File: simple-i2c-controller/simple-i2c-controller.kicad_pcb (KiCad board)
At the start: 2 copper layers, 10 parts, among them P1 CONN_VCC_IN, P2 I2C, P3 CONN_VCC, P4 CONN_5V, U1 ARDUINO_NANO

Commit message: [simple-i2c-controller]
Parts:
- moved P4 0.89 mm to (126.0, 54.6)
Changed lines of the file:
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@@
   )
   (module PINHEAD1-2-UP (layer F.Cu)
-    (at 125.095 54.61 90)
+    (at 125.984 54.61 90)
     (attr virtual)
     (fp_text reference P4 (at -1.905 -3.81 90) (layer F.SilkS)
@@
   (segment (start 131.826 56.896) (end 131.826 51.816) (width 0.508) (layer B.Cu) (net 1))
   (segment (start 133.35 58.42) (end 131.826 56.896) (width 0.508) (layer B.Cu) (net 1))
+  (segment (start 125.73 59.69) (end 125.73 59.436) (width 0.508) (layer B.Cu) (net 2))
+  (segment (start 128.651 56.515) (end 128.651 53.975) (width 0.508) (layer B.Cu) (net 2))
+  (segment (start 125.73 59.436) (end 128.651 56.515) (width 0.508) (layer B.Cu) (net 2))
   (segment (start 125.095 53.34) (end 122.936 53.34) (width 0.508) (layer B.Cu) (net 2))
   (segment (start 130.81 36.83) (end 130.81 33.02) (width 0.508) (layer B.Cu) (net 2))
@@
   (segment (start 122.936 53.34) (end 122.809 53.467) (width 0.508) (layer B.Cu) (net 2))
   (segment (start 125.095 53.34) (end 128.016 53.34) (width 0.508) (layer B.Cu) (net 2))
-  (segment (start 125.73 58.42) (end 125.73 59.69) (width 0.508) (layer B.Cu) (net 2))
-  (segment (start 128.651 55.499) (end 125.73 58.42) (width 0.508) (layer B.Cu) (net 2))
-  (segment (start 128.651 53.975) (end 128.651 55.499) (width 0.508) (layer B.Cu) (net 2))
   (segment (start 128.016 53.34) (end 128.651 53.975) (width 0.508) (layer B.Cu) (net 2))
   (segment (start 130.81 59.69) (end 130.81 57.785) (width 0.508) (layer B.Cu) (net 3))
@@
   (segment (start 123.317 49.53) (end 122.047 50.8) (width 0.508) (layer B.Cu) (net 4))
   (segment (start 126.873 49.53) (end 123.317 49.53) (width 0.508) (layer B.Cu) (net 4))
-  (segment (start 128.27 59.69) (end 128.27 57.785) (width 0.508) (layer B.Cu) (net 4))
+  (segment (start 128.27 59.69) (end 128.27 58.801) (width 0.508) (layer B.Cu) (net 4))
   (segment (start 122.047 50.8) (end 120.65 50.8) (width 0.508) (layer B.Cu) (net 4))
-  (segment (start 129.794 56.261) (end 129.794 52.451) (width 0.508) (layer B.Cu) (net 4))
-  (segment (start 128.27 57.785) (end 129.794 56.261) (width 0.508) (layer B.Cu) (net 4))
+  (segment (start 129.794 57.277) (end 129.794 52.451) (width 0.508) (layer B.Cu) (net 4))
+  (segment (start 128.27 58.801) (end 129.794 57.277) (width 0.508) (layer B.Cu) (net 4))
   (segment (start 134.62 55.88) (end 137.16 55.88) (width 1.27) (layer B.Cu) (net 5))
   (segment (start 132.715 40.005) (end 128.27 40.005) (width 1.27) (layer B.Cu) (net 5))

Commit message: [simple-i2c-controller] Added pull-up resistors to i2c bus.
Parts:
- added R1: 10k, R3-LARGE_PADS, F.Cu at (129.4, 50.4)
- added R2: 10k, R3-LARGE_PADS, F.Cu at (117.5, 44.5)
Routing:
- net +5V: track 43.7 -> 49.5 mm
- net N-0000025: track 19.4 -> 22.3 mm
- net VCC: track 44.1 -> 45.4 mm
- net N-000006: track 18.8 -> 17.6 mm
- net GND: track 72.1 -> 72.9 mm
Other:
- board text added: "SIMPLE I C Controller v1.1"
- board text removed: "SIMPLE I C Controller v1.0"

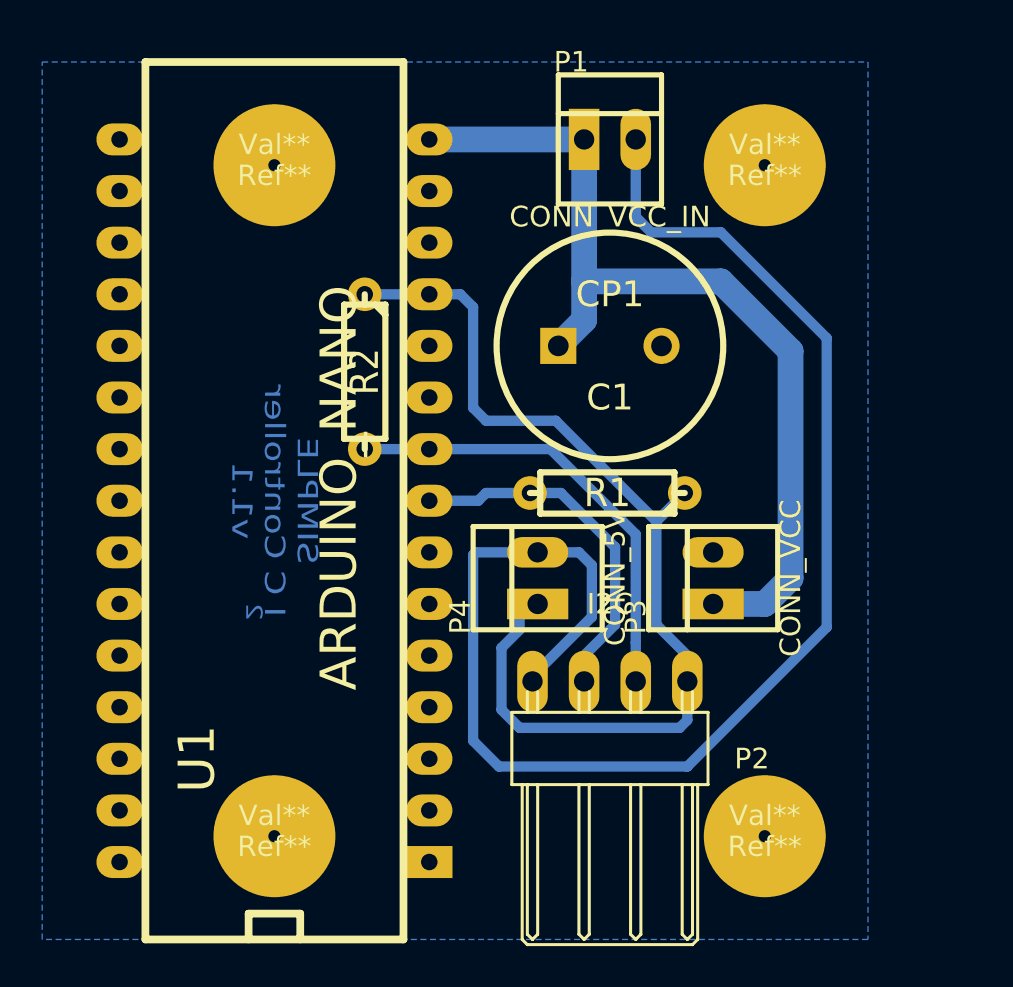
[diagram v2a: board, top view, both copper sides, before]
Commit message: [simple-i2c-controller] Screw holes enlarged and rearranged.
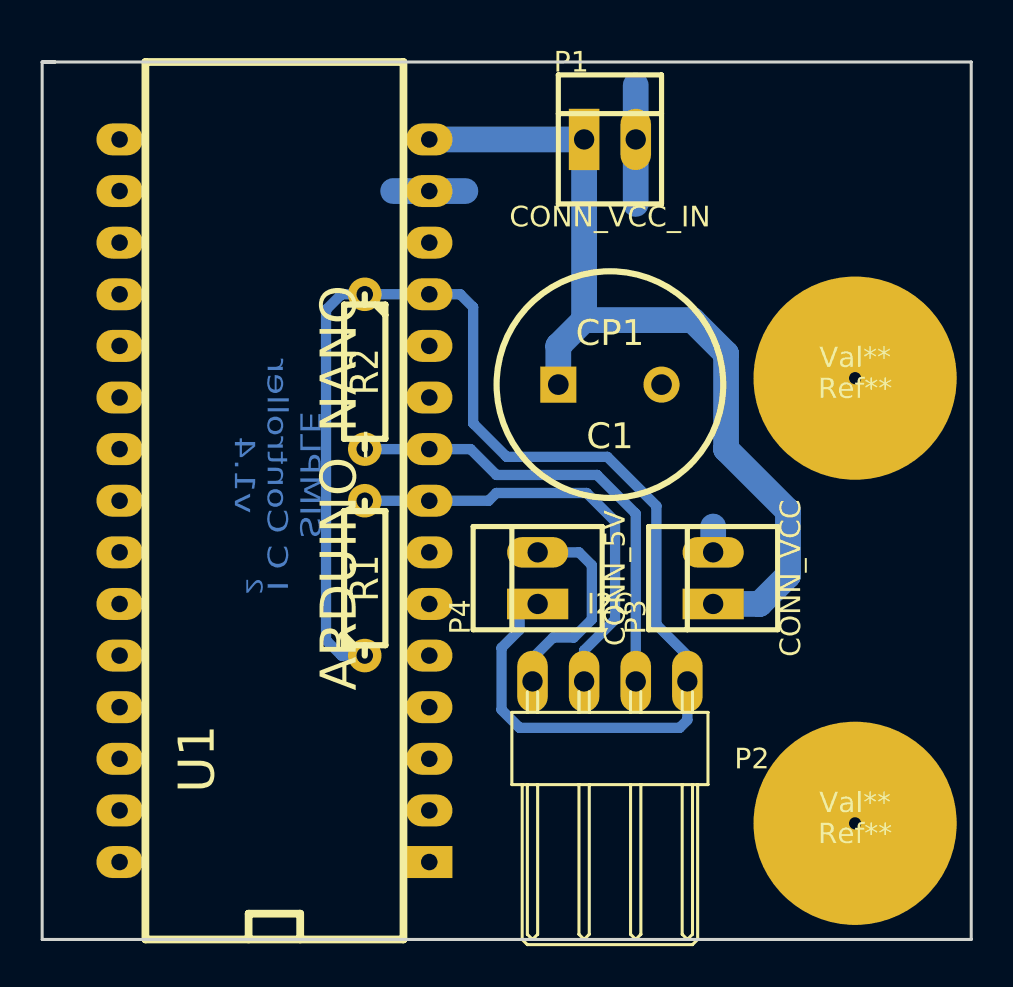
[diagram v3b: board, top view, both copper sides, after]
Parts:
- removed the Ref** at (113.0, 34.3)
- removed the Ref** at (137.2, 67.3)
- removed the Ref** at (113.0, 67.3)
- added Ref**: Val**, pad, F.Cu at (141.6, 66.7)
- moved R1 12.7 mm to (117.5, 54.6), turned to 90 degrees
- moved Ref** 11.4 mm to (141.6, 44.8)
- moved C1 1.91 mm to (129.5, 45.1)
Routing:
- net GND: track 72.9 -> 21.1 mm
- net +5V: track 49.5 -> 69.1 mm
- net N-000006: track 17.6 -> 21.6 mm
- net VCC: track 45.4 -> 44.3 mm
- net N-0000025: track 22.3 -> 22.9 mm
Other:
- board outline added: 45.7 x 43.2 mm
- net class Default: trace_width 0.508 -> 1.27
- board text added: "SIMPLE I C Controller v1.4"
- board text removed: "SIMPLE I C Controller v1.1"
